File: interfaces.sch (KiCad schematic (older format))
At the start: 76 parts, among them IC3 TPD8S009DSMR, J4 WE_629105150521, J6 685119134923, J7 1140084168, Q2 BSS138APW, Q3 BSS138APW, Q4 BSS138APW, Q5 BSS138APW, Q6 BSS138APW, U7 FT4232HQ, U8 SRST

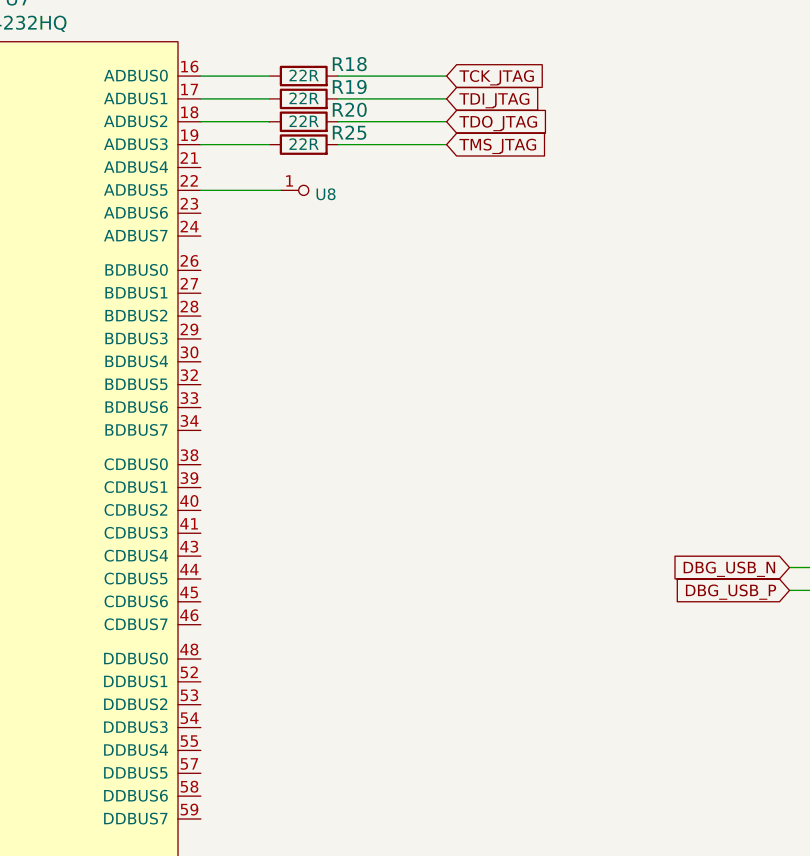
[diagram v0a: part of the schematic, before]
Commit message: Add aux JTAG connection to schematics
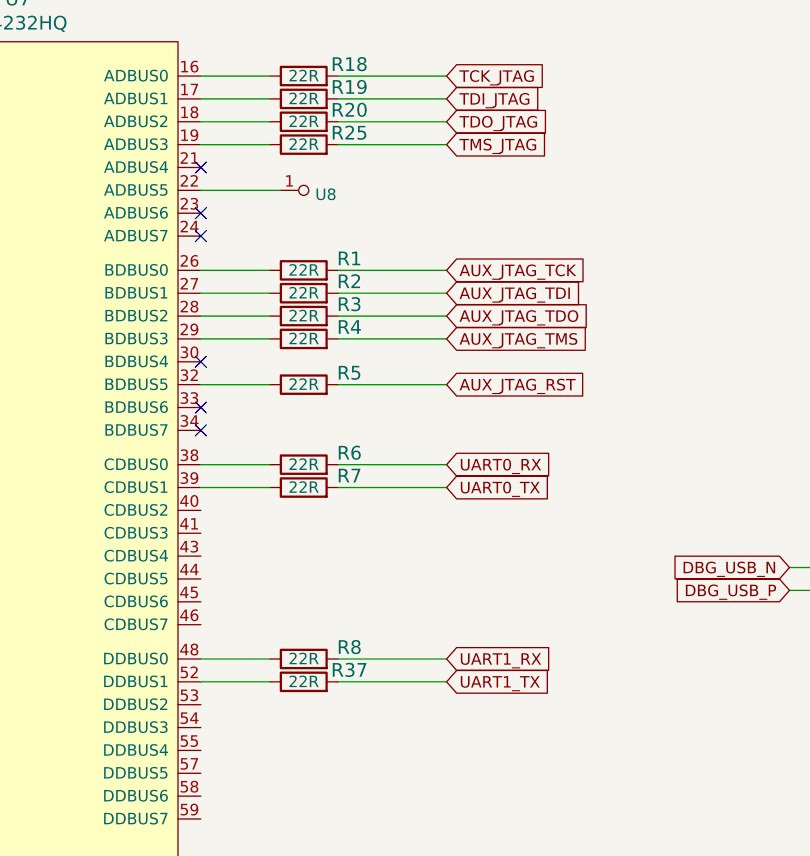
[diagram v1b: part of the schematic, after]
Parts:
- added R1, R2, R3, R37, R4, R5, R6, R7, R8: R_22R_0402, antmicro-footprints:0402-res, symbol antmicroResistors0402:R_22R_0402
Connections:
- net at U7.26 (BDBUS0): now also R1.1
- net at U7.27 (BDBUS1): now also R2.1
- net at U7.28 (BDBUS2): now also R3.1
- net at U7.29 (BDBUS3): now also R4.1
- net at U7.32 (BDBUS5): now also R5.1
- net at U7.38 (CDBUS0): now also R6.1
- net at U7.39 (CDBUS1): now also R7.1
- net at U7.48 (DDBUS0): now also R8.1
- net at U7.52 (DDBUS1): now also R37.1
- new net AUX_JTAG_RST: R5.2
- new net AUX_JTAG_TCK: R1.2
- new net AUX_JTAG_TDI: R2.2
- new net AUX_JTAG_TDO: R3.2
- new net AUX_JTAG_TMS: R4.2
- new net UART0_RX: R6.2
- new net UART0_TX: R7.2
- new net UART1_RX: R8.2
- new net UART1_TX: R37.2
- no-connect marks 1 -> 7
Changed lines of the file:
@@
 	3250 6800 3250 7350
-Wire Wire Line
-	3550 6800 3550 7350
 Wire Wire Line
 	3250 6400 3550 6400
@@
 User buttons
 $Comp
-L antmicroInterfaceControllers:FT4232HQ U7
-U 1 1 601044E5
-P 4350 5150
-F 0 "U7" H 4350 7637 60  0000 C CNN
-F 1 "FT4232HQ" H 4350 7531 60  0000 C CNN
-F 2 "antmicro-footprints:FT4232HQ" V 4550 5350 60  0001 L CNN
-F 3 "https://www.ftdichip.com/Support/Documents/DataSheets/ICs/DS_FT4232H.pdf" H 4550 5550 60  0001 L CNN
-F 4 "FTDI" H 4550 6300 60  0001 L CNN "Manufacturer"
-F 5 "FT4232HQ-TRAY" H 4550 5700 60  0001 L CNN "MPN"
-	1    4350 5150
-	1    0    0    -1
-$EndComp
-$Comp
 L antmicroResistors0402:R_22R_0402 R18
 U 1 1 6013A2FD
@@
 Text GLabel 5550 9525 2    50   Input ~ 0
 USR_BTN1
+$Comp
+L antmicroResistors0402:R_22R_0402 R1
+U 1 1 5FE0DD48
+P 5600 3850
+F 0 "R1" H 5800 3900 60  0000 C CNN
+F 1 "R_22R_0402" H 5600 3700 60  0001 C CNN
+F 2 "antmicro-footprints:0402-res" H 5800 4050 60  0001 L CNN
+F 3 "" H 5600 3850 50  0001 C CNN
+F 4 "VISHAY" H 5800 4250 60  0001 L CNN "Manufacturer"
+F 5 "CRCW040222R0FKED" H 5800 4150 60  0001 L CNN "MPN"
+F 6 "22R" H 5600 3850 50  0000 C CNN "Val"
+	1    5600 3850
+	1    0    0    -1
+$EndComp
+$Comp
+L antmicroResistors0402:R_22R_0402 R2
+U 1 1 5FE0E0D9
+P 5600 3950
+F 0 "R2" H 5800 4000 60  0000 C CNN
+F 1 "R_22R_0402" H 5600 3800 60  0001 C CNN
+F 2 "antmicro-footprints:0402-res" H 5800 4150 60  0001 L CNN
+F 3 "" H 5600 3950 50  0001 C CNN
+F 4 "VISHAY" H 5800 4350 60  0001 L CNN "Manufacturer"
+F 5 "CRCW040222R0FKED" H 5800 4250 60  0001 L CNN "MPN"
+F 6 "22R" H 5600 3950 50  0000 C CNN "Val"
+	1    5600 3950
+	1    0    0    -1
+$EndComp
+$Comp
+L antmicroResistors0402:R_22R_0402 R4
+U 1 1 5FE0E52B
+P 5600 4150
+F 0 "R4" H 5800 4200 60  0000 C CNN
+F 1 "R_22R_0402" H 5600 4000 60  0001 C CNN
+F 2 "antmicro-footprints:0402-res" H 5800 4350 60  0001 L CNN
+F 3 "" H 5600 4150 50  0001 C CNN
+F 4 "VISHAY" H 5800 4550 60  0001 L CNN "Manufacturer"
+F 5 "CRCW040222R0FKED" H 5800 4450 60  0001 L CNN "MPN"
+F 6 "22R" H 5600 4150 50  0000 C CNN "Val"
+	1    5600 4150
+	1    0    0    -1
+$EndComp
+$Comp
+L antmicroResistors0402:R_22R_0402 R3
+U 1 1 5FE0E30A
+P 5600 4050
+F 0 "R3" H 5800 4100 60  0000 C CNN
+F 1 "R_22R_0402" H 5600 3900 60  0001 C CNN
+F 2 "antmicro-footprints:0402-res" H 5800 4250 60  0001 L CNN
+F 3 "" H 5600 4050 50  0001 C CNN
+F 4 "VISHAY" H 5800 4450 60  0001 L CNN "Manufacturer"
+F 5 "CRCW040222R0FKED" H 5800 4350 60  0001 L CNN "MPN"
+F 6 "22R" H 5600 4050 50  0000 C CNN "Val"
+	1    5600 4050
+	1    0    0    -1
+$EndComp
+Wire Wire Line
+	5450 3850 5150 3850
+Wire Wire Line
+	5450 3950 5150 3950
+Wire Wire Line
+	5450 4050 5150 4050
+Wire Wire Line
+	5450 4150 5150 4150
+Wire Wire Line
+	5750 3850 6225 3850
+Wire Wire Line
+	5750 3950 6225 3950
+Wire Wire Line
+	5750 4050 6225 4050
+Wire Wire Line
+	5750 4150 6225 4150
+Text GLabel 6225 3950 2    50   Input ~ 0
+AUX_JTAG_TDI
+Text GLabel 6225 4050 2    50   Input ~ 0
+AUX_JTAG_TDO
+Text GLabel 6225 4150 2    50   Input ~ 0
+AUX_JTAG_TMS
+Text GLabel 6225 4700 2    50   Input ~ 0
+UART0_RX
+Text GLabel 6225 5550 2    50   Input ~ 0
+UART1_RX
+$Comp
+L antmicroResistors0402:R_22R_0402 R6
+U 1 1 5FEB07CF
+P 5600 4700
+F 0 "R6" H 5800 4750 60  0000 C CNN
+F 1 "R_22R_0402" H 5600 4550 60  0001 C CNN
+F 2 "antmicro-footprints:0402-res" H 5800 4900 60  0001 L CNN
+F 3 "" H 5600 4700 50  0001 C CNN
+F 4 "VISHAY" H 5800 5100 60  0001 L CNN "Manufacturer"
+F 5 "CRCW040222R0FKED" H 5800 5000 60  0001 L CNN "MPN"
+F 6 "22R" H 5600 4700 50  0000 C CNN "Val"
+	1    5600 4700
+	1    0    0    -1
+$EndComp
+$Comp
+L antmicroResistors0402:R_22R_0402 R37
+U 1 1 5FEB0AF8
+P 5600 5650
+F 0 "R37" H 5800 5700 60  0000 C CNN
+F 1 "R_22R_0402" H 5600 5500 60  0001 C CNN
+F 2 "antmicro-footprints:0402-res" H 5800 5850 60  0001 L CNN
+F 3 "" H 5600 5650 50  0001 C CNN
+F 4 "VISHAY" H 5800 6050 60  0001 L CNN "Manufacturer"
+F 5 "CRCW040222R0FKED" H 5800 5950 60  0001 L CNN "MPN"
+F 6 "22R" H 5600 5650 50  0000 C CNN "Val"
+	1    5600 5650
+	1    0    0    -1
+$EndComp
+Text GLabel 6225 4800 2    50   Input ~ 0
+UART0_TX
+Text GLabel 6225 5650 2    50   Input ~ 0
+UART1_TX
+$Comp
+L antmicroResistors0402:R_22R_0402 R7
+U 1 1 5FEB126C
+P 5600 4800
+F 0 "R7" H 5800 4850 60  0000 C CNN
+F 1 "R_22R_0402" H 5600 4650 60  0001 C CNN
+F 2 "antmicro-footprints:0402-res" H 5800 5000 60  0001 L CNN
+F 3 "" H 5600 4800 50  0001 C CNN
+F 4 "VISHAY" H 5800 5200 60  0001 L CNN "Manufacturer"
+F 5 "CRCW040222R0FKED" H 5800 5100 60  0001 L CNN "MPN"
+F 6 "22R" H 5600 4800 50  0000 C CNN "Val"
+	1    5600 4800
+	1    0    0    -1
+$EndComp
+$Comp
+L antmicroResistors0402:R_22R_0402 R8
+U 1 1 5FEB1585
+P 5600 5550
+F 0 "R8" H 5800 5600 60  0000 C CNN
+F 1 "R_22R_0402" H 5600 5400 60  0001 C CNN
+F 2 "antmicro-footprints:0402-res" H 5800 5750 60  0001 L CNN
+F 3 "" H 5600 5550 50  0001 C CNN
+F 4 "VISHAY" H 5800 5950 60  0001 L CNN "Manufacturer"
+F 5 "CRCW040222R0FKED" H 5800 5850 60  0001 L CNN "MPN"
+F 6 "22R" H 5600 5550 50  0000 C CNN "Val"
+	1    5600 5550
+	1    0    0    -1
+$EndComp
+Wire Wire Line
+	5150 5550 5450 5550
+Wire Wire Line
+	5150 5650 5450 5650
+Wire Wire Line
+	5150 4800 5450 4800
+Wire Wire Line
+	5150 4700 5450 4700
+Wire Wire Line
+	5750 4700 6225 4700
+Wire Wire Line
+	5750 5550 6225 5550
+Wire Wire Line
+	5750 5650 6225 5650
+Wire Wire Line
+	6225 4800 5750 4800
+Text GLabel 6225 3850 2    50   Input ~ 0
+AUX_JTAG_TCK
+$Comp
+L antmicroResistors0402:R_22R_0402 R5
+U 1 1 601136B0
+P 5600 4350
+F 0 "R5" H 5800 4400 60  0000 C CNN
+F 1 "R_22R_0402" H 5600 4200 60  0001 C CNN
+F 2 "antmicro-footprints:0402-res" H 5800 4550 60  0001 L CNN
+F 3 "" H 5600 4350 50  0001 C CNN
+F 4 "VISHAY" H 5800 4750 60  0001 L CNN "Manufacturer"
+F 5 "CRCW040222R0FKED" H 5800 4650 60  0001 L CNN "MPN"
+F 6 "22R" H 5600 4350 50  0000 C CNN "Val"
+	1    5600 4350
+	1    0    0    -1
+$EndComp
+Wire Wire Line
+	5450 4350 5150 4350
+Wire Wire Line
+	5750 4350 6225 4350
+Text GLabel 6225 4350 2    50   Input ~ 0
+AUX_JTAG_RST
+Wire Wire Line
+	3550 6800 3550 7350
+$Comp
+L antmicroInterfaceControllers:FT4232HQ U7
+U 1 1 601044E5
+P 4350 5150
+F 0 "U7" H 4350 7637 60  0000 C CNN
+F 1 "FT4232HQ" H 4350 7531 60  0000 C CNN
+F 2 "antmicro-footprints:FT4232HQ" V 4550 5350 60  0001 L CNN
+F 3 "https://www.ftdichip.com/Support/Documents/DataSheets/ICs/DS_FT4232H.pdf" H 4550 5550 60  0001 L CNN
+F 4 "FTDI" H 4550 6300 60  0001 L CNN "Manufacturer"
+F 5 "FT4232HQ-TRAY" H 4550 5700 60  0001 L CNN "MPN"
+	1    4350 5150
+	1    0    0    -1
+$EndComp
+NoConn ~ 5150 3400
+NoConn ~ 5150 3600
+NoConn ~ 5150 3700
+NoConn ~ 5150 4250
+NoConn ~ 5150 4450
+NoConn ~ 5150 4550
 $EndSCHEMATC

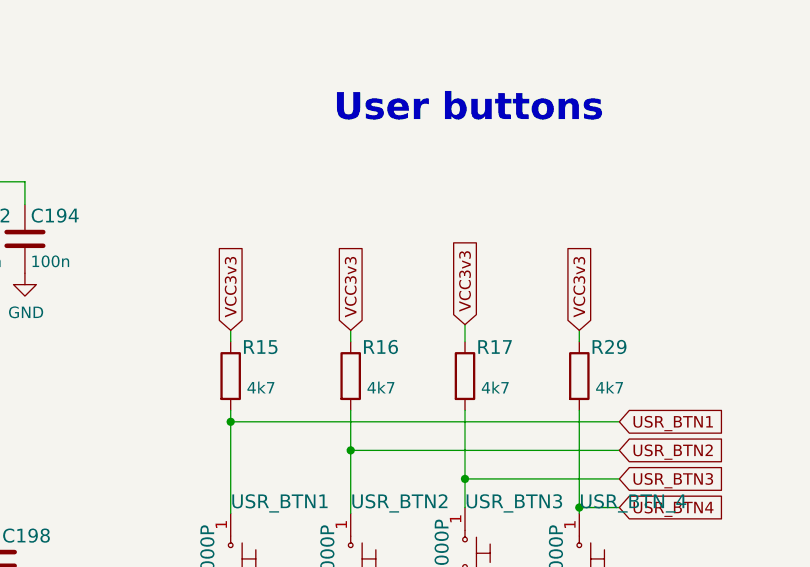
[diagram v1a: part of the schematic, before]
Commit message: Fix VCC labels
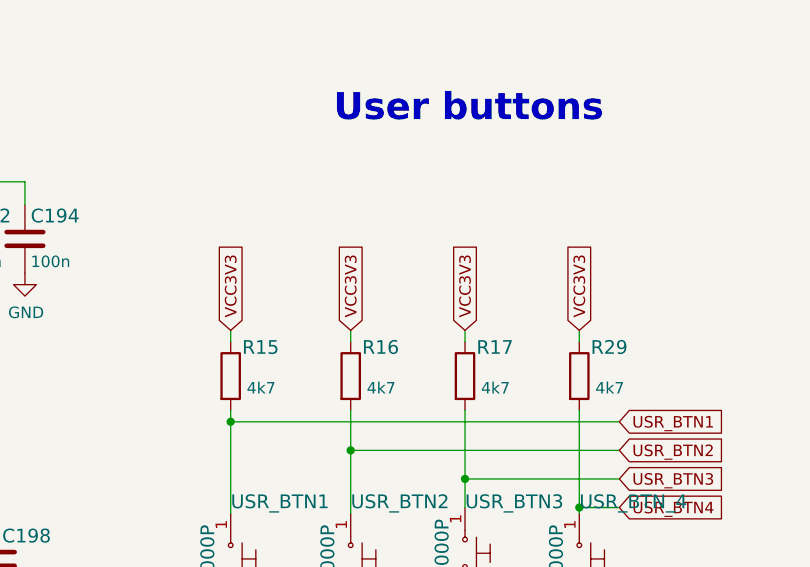
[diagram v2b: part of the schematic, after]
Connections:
- net VCC3v3 is gone; now on net VCC3V3: R15.1, R16.1, R17.1, R29.1
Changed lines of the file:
@@
 	1    0    0    -1
 $EndComp
-Text GLabel 4375 9125 1    50   Input ~ 0
-VCC3v3
 $Comp
 L lpddr4-test-board:R_4k7_0402 R?
@@
 	0    1    1    0
 $EndComp
-Text GLabel 3850 9125 1    50   Input ~ 0
-VCC3v3
 $Comp
 L lpddr4-test-board:GND #PWR?
@@
 	4875 9775 5550 9775
 Wire Wire Line
-	4875 9100 4875 9175
+	4875 9125 4875 9175
 $Comp
 L lpddr4-test-board:R_4k7_0402 R?
@@
 	0    1    1    0
 $EndComp
-Text GLabel 4875 9100 1    50   Input ~ 0
-VCC3v3
 Text Notes 4300 8225 0    118  ~ 24
 User buttons
@@
 	0    1    1    0
 $EndComp
-Text GLabel 5375 9125 1    50   Input ~ 0
-VCC3v3
 $Comp
 L lpddr4-test-board:GND #PWR?
@@
 NoConn ~ 5150 4450
 NoConn ~ 5150 4550
+Text GLabel 3850 9125 1    50   Input ~ 0
+VCC3V3
+Text GLabel 4375 9125 1    50   Input ~ 0
+VCC3V3
+Text GLabel 4875 9125 1    50   Input ~ 0
+VCC3V3
+Text GLabel 5375 9125 1    50   Input ~ 0
+VCC3V3
 $EndSCHEMATC

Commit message: Update RGMII connector, started DRAM DQ equalization
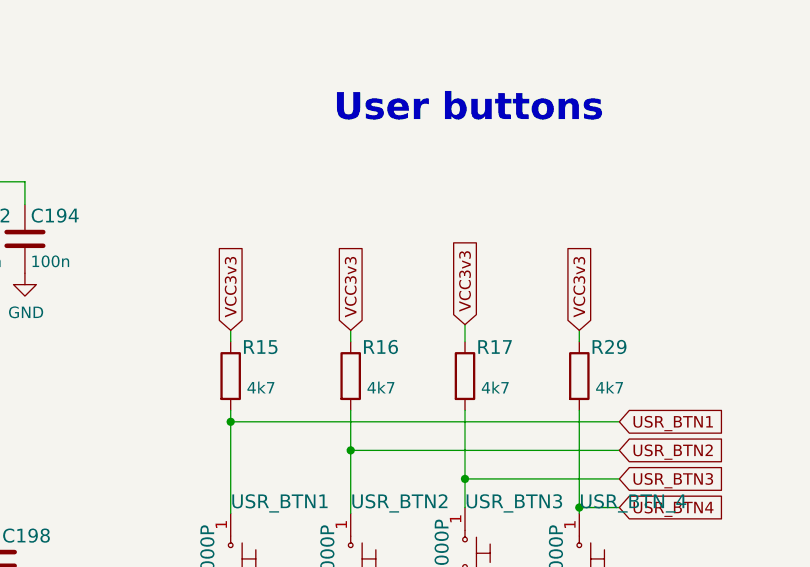
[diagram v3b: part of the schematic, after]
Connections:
- net VCC3V3: no longer R15.1, R16.1, R17.1, R29.1
- new net VCC3v3: R15.1, R16.1, R17.1, R29.1
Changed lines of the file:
@@
 	1    0    0    -1
 $EndComp
+Text GLabel 4375 9125 1    50   Input ~ 0
+VCC3v3
 $Comp
 L lpddr4-test-board:R_4k7_0402 R?
@@
 	0    1    1    0
 $EndComp
+Text GLabel 3850 9125 1    50   Input ~ 0
+VCC3v3
 $Comp
 L lpddr4-test-board:GND #PWR?
@@
 	4875 9775 5550 9775
 Wire Wire Line
-	4875 9125 4875 9175
+	4875 9100 4875 9175
 $Comp
 L lpddr4-test-board:R_4k7_0402 R?
@@
 	0    1    1    0
 $EndComp
+Text GLabel 4875 9100 1    50   Input ~ 0
+VCC3v3
 Text Notes 4300 8225 0    118  ~ 24
 User buttons
@@
 	0    1    1    0
 $EndComp
+Text GLabel 5375 9125 1    50   Input ~ 0
+VCC3v3
 $Comp
 L lpddr4-test-board:GND #PWR?
@@
 NoConn ~ 5150 4450
 NoConn ~ 5150 4550
-Text GLabel 3850 9125 1    50   Input ~ 0
-VCC3V3
-Text GLabel 4375 9125 1    50   Input ~ 0
-VCC3V3
-Text GLabel 4875 9125 1    50   Input ~ 0
-VCC3V3
-Text GLabel 5375 9125 1    50   Input ~ 0
-VCC3V3
 $EndSCHEMATC

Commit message: Fix labels
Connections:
- net VCC3v3 is gone; now on net VCC3V3: R15.1, R16.1, R17.1, R29.1
- net VCC1V8 renamed VDD1V8
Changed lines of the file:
@@
 	1    0    0    -1
 $EndComp
-Text GLabel 2375 9775 1    50   Input ~ 0
-VCC1V8
 Wire Wire Line
 	1750 8575 1750 8475
@@
 	2375 9875 2225 9875
 Text GLabel 3300 2750 1    50   Input ~ 0
-VCC1V8
+VDD1V8
 Text GLabel 3450 2750 1    50   Input ~ 0
 VCC3V3
@@
 	1    0    0    -1
 $EndComp
-Text GLabel 4375 9125 1    50   Input ~ 0
-VCC3v3
 $Comp
 L lpddr4-test-board:R_4k7_0402 R?
@@
 	0    1    1    0
 $EndComp
-Text GLabel 3850 9125 1    50   Input ~ 0
-VCC3v3
 $Comp
 L lpddr4-test-board:GND #PWR?
@@
 	0    1    1    0
 $EndComp
-Text GLabel 4875 9100 1    50   Input ~ 0
-VCC3v3
 Text Notes 4300 8225 0    118  ~ 24
 User buttons
@@
 	0    1    1    0
 $EndComp
-Text GLabel 5375 9125 1    50   Input ~ 0
-VCC3v3
 $Comp
 L lpddr4-test-board:GND #PWR?
@@
 NoConn ~ 5150 4450
 NoConn ~ 5150 4550
+Text GLabel 2375 9775 1    50   Input ~ 0
+VDD1V8
+Text GLabel 3850 9125 1    50   Input ~ 0
+VCC3V3
+Text GLabel 4375 9125 1    50   Input ~ 0
+VCC3V3
+Text GLabel 4875 9100 1    50   Input ~ 0
+VCC3V3
+Text GLabel 5375 9125 1    50   Input ~ 0
+VCC3V3
 $EndSCHEMATC

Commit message: Add crystal
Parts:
- added Y?: ABM8G-12.000MHZ-18-D2Y-T, antmicro-footprints:KX-7, symbol antmicroCrystals:ABM8G-12.000MHZ-18-D2Y-T
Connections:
- net GND: now also Y?.2, Y?.4
- net at C190.1, U7.2 (OSCI): now also Y?.1
- net at C193.1, U7.3 (OSCO): now also Y?.3
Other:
- note removed: "TODO: add QC3A12"
- moved on the sheet: C190, C193
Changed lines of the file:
@@
 Wire Wire Line
 	3150 5400 3050 5400
-Text Notes 1075 6050 0    118  ~ 24
-TODO: add QC3A12
-Wire Wire Line
-	2450 6200 2450 6500
-Wire Wire Line
-	3250 6400 3250 6500
+Wire Wire Line
+	2450 6200 2450 6550
+Wire Wire Line
+	3250 6400 3250 6550
 $Comp
 L lpddr4-test-board:C_18p_0402 C190
 U 1 1 5FFDD1FF
-P 2450 6650
-F 0 "C190" H 2475 6750 60  0000 L CNN
-F 1 "C_18p_0402" H 2450 6500 60  0001 C CNN
-F 2 "lpddr4-test-board-footprints:0402-cap" H 2650 6850 60  0001 L CNN
-F 3 "" H 2450 6650 50  0001 C CNN
-F 4 "MULTICOMP" H 2650 7050 60  0001 L CNN "Manufacturer"
-F 5 "MC0402N180J500CT" H 2650 6950 60  0001 L CNN "MPN"
-F 6 "18p" H 2475 6550 50  0000 L CNN "Val"
-	1    2450 6650
+P 2450 6950
+F 0 "C190" H 2475 7050 60  0000 L CNN
+F 1 "C_18p_0402" H 2450 6800 60  0001 C CNN
+F 2 "lpddr4-test-board-footprints:0402-cap" H 2650 7150 60  0001 L CNN
+F 3 "" H 2450 6950 50  0001 C CNN
+F 4 "MULTICOMP" H 2650 7350 60  0001 L CNN "Manufacturer"
+F 5 "MC0402N180J500CT" H 2650 7250 60  0001 L CNN "MPN"
+F 6 "18p" H 2475 6850 50  0000 L CNN "Val"
+	1    2450 6950
 	1    0    0    -1
 $EndComp
@@
 L lpddr4-test-board:C_18p_0402 C193
 U 1 1 5FFDD6CC
-P 3250 6650
-F 0 "C193" H 3275 6750 60  0000 L CNN
-F 1 "C_18p_0402" H 3250 6500 60  0001 C CNN
-F 2 "lpddr4-test-board-footprints:0402-cap" H 3450 6850 60  0001 L CNN
-F 3 "" H 3250 6650 50  0001 C CNN
-F 4 "MULTICOMP" H 3450 7050 60  0001 L CNN "Manufacturer"
-F 5 "MC0402N180J500CT" H 3450 6950 60  0001 L CNN "MPN"
-F 6 "18p" H 3275 6550 50  0000 L CNN "Val"
-	1    3250 6650
+P 3250 6950
+F 0 "C193" H 3275 7050 60  0000 L CNN
+F 1 "C_18p_0402" H 3250 6800 60  0001 C CNN
+F 2 "lpddr4-test-board-footprints:0402-cap" H 3450 7150 60  0001 L CNN
+F 3 "" H 3250 6950 50  0001 C CNN
+F 4 "MULTICOMP" H 3450 7350 60  0001 L CNN "Manufacturer"
+F 5 "MC0402N180J500CT" H 3450 7250 60  0001 L CNN "MPN"
+F 6 "18p" H 3275 6850 50  0000 L CNN "Val"
+	1    3250 6950
 	1    0    0    -1
 $EndComp
@@
 $EndComp
 Wire Wire Line
-	2450 6800 2450 7350
-Wire Wire Line
-	3250 6800 3250 7350
+	2450 7100 2450 7350
+Wire Wire Line
+	3250 7100 3250 7350
 Wire Wire Line
 	3250 6400 3550 6400
@@
 Text GLabel 5375 9125 1    50   Input ~ 0
 VCC3V3
+$Comp
+L antmicroCrystals:ABM8G-12.000MHZ-18-D2Y-T Y?
+U 1 1 61D2EA50
+P 2875 6550
+F 0 "Y?" H 3069 6643 31  0000 L CNN
+F 1 "ABM8G-12.000MHZ-18-D2Y-T" H 3069 6581 31  0000 L CNN
+F 2 "antmicro-footprints:KX-7" H 4975 6550 50  0001 C CNN
+F 3 "" H 5075 6650 50  0001 C CNN
+F 4 "ABM8G-12.000MHZ-18-D2Y-T " H 3069 6519 31  0000 L CNN "MPN"
+F 5 "Abracon" H 3069 6457 31  0000 L CNN "Manufacturer"
+	1    2875 6550
+	1    0    0    -1
+$EndComp
+Wire Wire Line
+	3025 6550 3250 6550
+Connection ~ 3250 6550
+Wire Wire Line
+	3250 6550 3250 6800
+Wire Wire Line
+	2725 6550 2450 6550
+Connection ~ 2450 6550
+Wire Wire Line
+	2450 6550 2450 6800
+Wire Wire Line
+	2875 6750 2875 7350
+$Comp
+L lpddr4-test-board:GND #PWR?
+U 1 1 61E026BC
+P 2875 7350
+F 0 "#PWR?" H 2875 7100 50  0001 C CNN
+F 1 "GND" H 2880 7177 50  0000 C CNN
+F 2 "" H 2875 7350 50  0001 C CNN
+F 3 "" H 2875 7350 50  0001 C CNN
+	1    2875 7350
+	1    0    0    -1
+$EndComp
+$Comp
+L lpddr4-test-board:GND #PWR?
+U 1 1 61E1A1A0
+P 2875 6350
+F 0 "#PWR?" H 2875 6100 50  0001 C CNN
+F 1 "GND" H 2725 6275 50  0000 C CNN
+F 2 "" H 2875 6350 50  0001 C CNN
+F 3 "" H 2875 6350 50  0001 C CNN
+	1    2875 6350
+	-1   0    0    1
+$EndComp
 $EndSCHEMATC
